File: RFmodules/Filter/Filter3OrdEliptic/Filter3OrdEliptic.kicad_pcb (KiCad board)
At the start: 2 copper layers, 37.5 x 9.5 mm, 11 parts, among them J1 SMA, J2 SMA

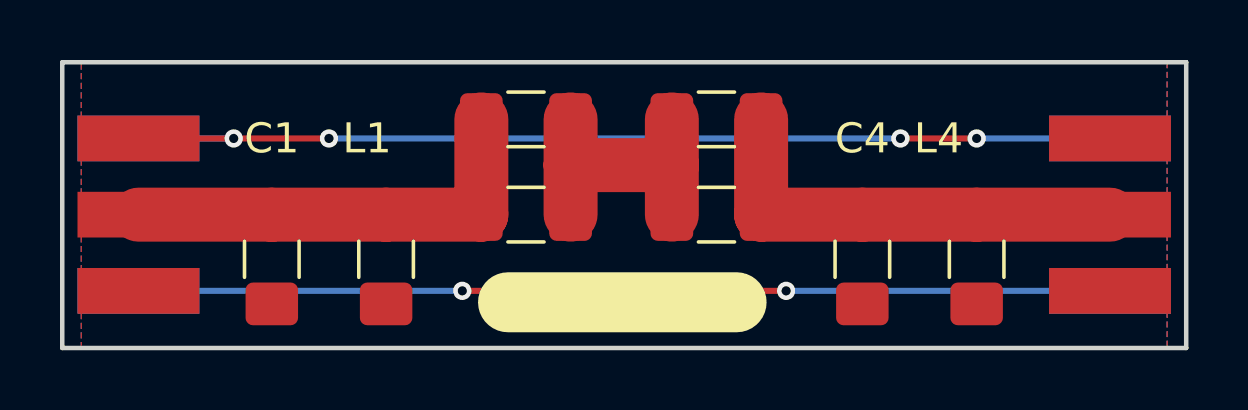
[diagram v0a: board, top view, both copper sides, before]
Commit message: Fix 3th order elliptic bandpass filter labels
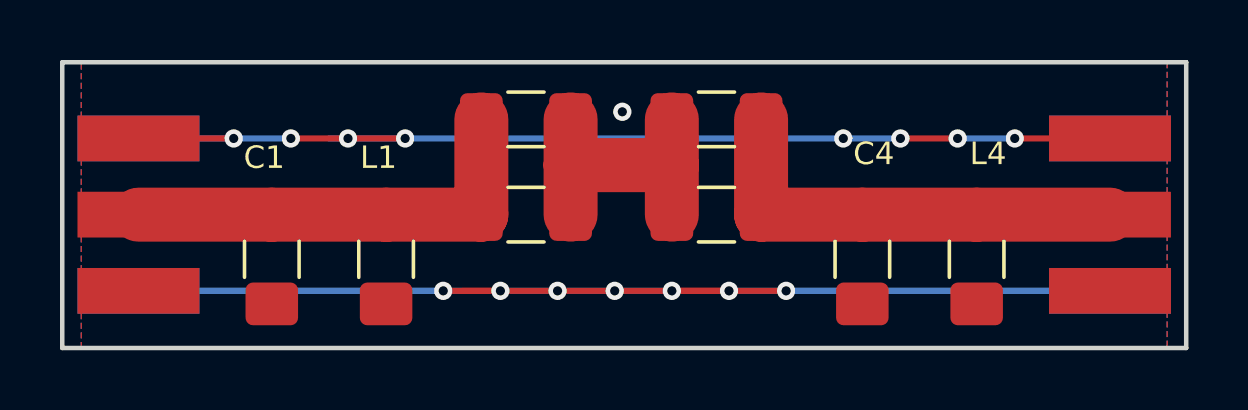
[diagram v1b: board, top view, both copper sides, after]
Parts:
- moved REF** 9.60 mm to (108.6, 95.4)
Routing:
- net GND: track 67.9 -> 102.9 mm, vias 6 -> 16
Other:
- board text added: "3th Order Elliptic Bandpass Filter"
- board text added: "Revision v0.1.0"
- board text added: "github.com/fgaletsee/RFLego"

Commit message: Update board descriptions, add Bandstop elliptic filter 5th order
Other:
- board text added: "Bandpass Filter Elliptic 3th Order Revision 1 - 01/2019 github.com/fgaletsee/RFLego"
- board text removed: "3th Order Elliptic Bandpass Filter"
- board text removed: "Revision v0.1.0"
- board text removed: "github.com/fgaletsee/RFLego"
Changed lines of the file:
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@@
   (general
     (thickness 1.6)
-    (drawings 8)
+    (drawings 6)
     (tracks 55)
     (zones 0)
@@
     (last_trace_width 0.2032)
     (trace_clearance 0.2032)
-    (zone_clearance 0.508)
+    (zone_clearance 0.1)
     (zone_45_only no)
     (trace_min 0.2032)
@@
       (xy -2.549664 -1.91989) (xy -2.469928 -1.911165) (xy -2.400256 -1.919918)) (layer B.SilkS) (width 0.01))
   )
-  (gr_text github.com/fgaletsee/RFLego (at 119.634 93.345) (layer B.SilkS)
-    (effects (font (size 0.5 0.5) (thickness 0.125)) (justify mirror))
-  )
-  (gr_text "Revision v0.1.0" (at 122.428 92.329) (layer B.SilkS)
-    (effects (font (size 0.5 0.5) (thickness 0.125)) (justify mirror))
-  )
-  (gr_text "3th Order Elliptic  Bandpass Filter" (at 118.8212 91.29268) (layer B.SilkS)
-    (effects (font (size 0.5 0.5) (thickness 0.125)) (justify mirror))
+  (gr_text "Bandpass Filter Elliptic 3th Order\nRevision 1 - 01/2019\ngithub.com/fgaletsee/RFLego" (at 132.1816 94.1578) (layer B.SilkS)
+    (effects (font (size 0.75 0.75) (thickness 0.1875)) (justify left mirror))
   )
   (gr_line (start 99.695 99.06) (end 99.695 89.535) (layer Edge.Cuts) (width 0.15))
@@
   (gr_line (start 137.16 89.535) (end 137.16 99.06) (layer Edge.Cuts) (width 0.15))
   (gr_line (start 99.695 89.535) (end 137.16 89.535) (layer Edge.Cuts) (width 0.15))
-  (gr_line (start 112.776 95.25) (end 124.206 95.25) (layer B.SilkS) (width 2))
+  (gr_line (start 113.8682 97.1804) (end 125.2982 97.1804) (layer B.SilkS) (width 2))
   (segment (start 102.235 94.615) (end 106.68 94.615) (width 1.8) (layer F.Cu) (net 1))
   (segment (start 106.68 94.615) (end 110.49 94.615) (width 1.8) (layer F.Cu) (net 1))
@@
   (segment (start 130.175 94.615) (end 134.62 94.615) (width 1.8) (layer F.Cu) (net 4))
   (zone (net 2) (net_name GND) (layer F.Cu) (hatch edge 0.508)
-    (connect_pads (clearance 0.508))
+    (connect_pads yes (clearance 0.1))
     (min_thickness 0.254)
     (fill yes (arc_segments 16) (thermal_gap 0.508) (thermal_bridge_width 0.508))
@@
   )
   (zone (net 2) (net_name GND) (layer B.Cu) (hatch edge 0.508)
-    (connect_pads (clearance 0.508))
+    (connect_pads yes (clearance 0.1))
     (min_thickness 0.254)
     (fill yes (arc_segments 16) (thermal_gap 0.508) (thermal_bridge_width 0.508))
